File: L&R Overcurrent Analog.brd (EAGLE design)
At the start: 55 x 55 mm, 22 parts, among them IC1 CSLA2CFTH, IC2 TLC393CPN, IC3 7805TV, Q1 SUP75P0307, Q2 SUP75P0307, X1 J1

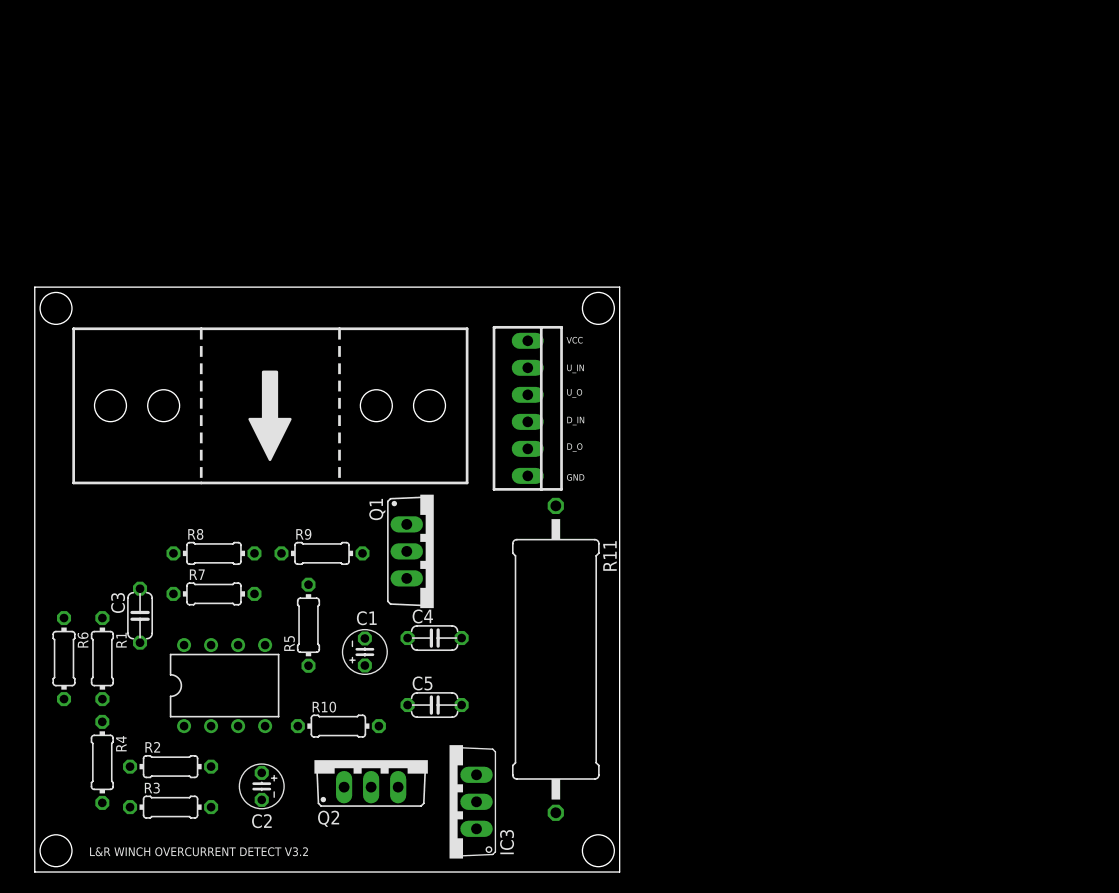
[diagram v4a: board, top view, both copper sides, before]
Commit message: Split transducer from main board, added schematic frame.
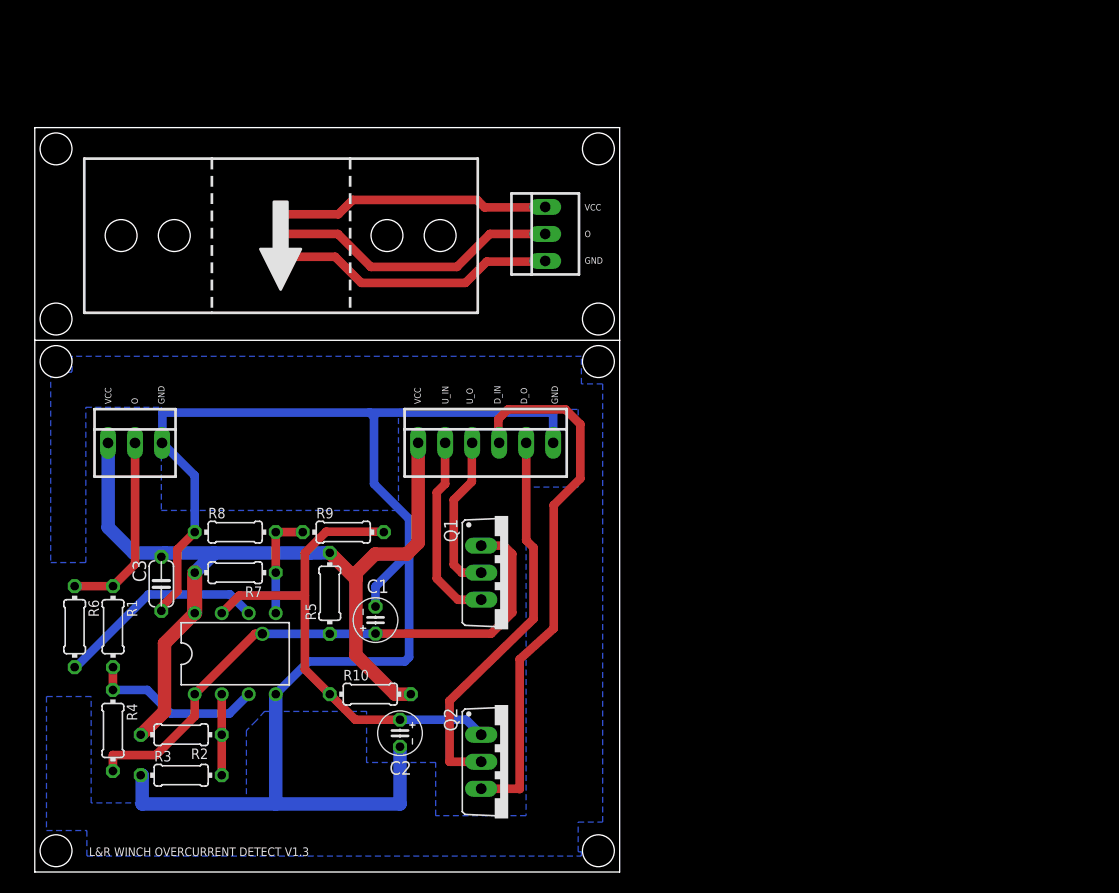
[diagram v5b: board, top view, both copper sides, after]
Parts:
- removed C4: 0.33u, Overcurrent Detect:C050-024X044
- removed C5: 0.1u, Overcurrent Detect:C050-024X044
- removed IC3: 7805TV, Overcurrent Detect:TO220V
- removed R11: 2, Overcurrent Detect:0617/22
- added X2: J2, Overcurrent Detect:22-23-2031
- added X3: J3, Overcurrent Detect:22-23-2031
- C1: value 20u -> 22u
- C2: value 20u -> 22u\
- moved IC1 16.0 mm to (23.1, 59.9)
- moved C2 13.9 mm to (34.3, 13.1)
- moved Q2 12.9 mm to (44.5, 10.4), turned to 270 degrees
- moved Q1 7.28 mm to (44.5, 28.1)
- moved X1 5.12 mm to (42.4, 40.4), turned to 0 degrees
- moved R10 4.24 mm to (31.6, 16.7)
- moved C3 3.61 mm to (11.9, 27.1)
- moved R5 3.61 mm to (27.7, 26.2)
- moved C1 3.16 mm to (32.0, 23.7)
- moved IC2 3.16 mm to (18.9, 20.5)
- moved R1 3.16 mm to (7.36, 23.1)
- moved R2 3.16 mm to (13.8, 12.9)
- moved R3 3.16 mm to (13.8, 9.10)
- moved R4 3.16 mm to (7.35, 13.3)
- moved R6 3.16 mm to (3.75, 23.1)
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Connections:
- removed net +5V: C3.1, C5.1, IC1.V+, IC2.8, IC3.3, R10.2, R2.2, R5.2, R7.2
- removed net N$3: IC1.O, R1.1, R6.1
- new net N$13: IC1.V-, X3.3
- new net N$14: IC1.O, X3.2
- new net N$15: R1.1, R6.1, X2.2
- net +12V: now also C3.1, IC2.8, R10.2, R2.2, R5.2, R7.2, X2.1; no longer R11.1
- net GND: now also X2.3; no longer C4.2, C5.2, IC1.V-, IC3.2
- net N$12: now also IC1.V+, X3.1; no longer C4.1, IC3.1, R11.2
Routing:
- net GND: track 0.00 -> 148.5 mm
- net +12V: track 0.00 -> 84.6 mm
- net N$6: track 0.00 -> 54.6 mm, vias 0 -> 1
- net N$10: track 0.00 -> 51.3 mm
- net N$7: track 0.00 -> 46.9 mm
- net N$11: track 0.00 -> 36.6 mm
- net N$14: track 0.00 -> 27.5 mm
- net N$12: track 0.00 -> 26.7 mm
- net N$13: track 0.00 -> 25.7 mm
- net N$4: track 0.00 -> 19.9 mm
- net N$8: track 0.00 -> 18.1 mm
- net N$15: track 0.00 -> 17.9 mm
- net N$1: track 0.00 -> 16.6 mm
- net N$9: track 0.00 -> 15.1 mm
- net N$5: track 0.00 -> 10.2 mm
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- added copper zone on layer 16, net GND
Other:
- board size 55 x 55 mm -> 55 x 70 mm
- board text added: "L&R WINCH OVERCURRENT DETECT V1.3"
- board text added: "O"
- board text removed: "L&R WINCH OVERCURRENT DETECT V3.2"

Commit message: Updated / added document frames and added cutout to PCB
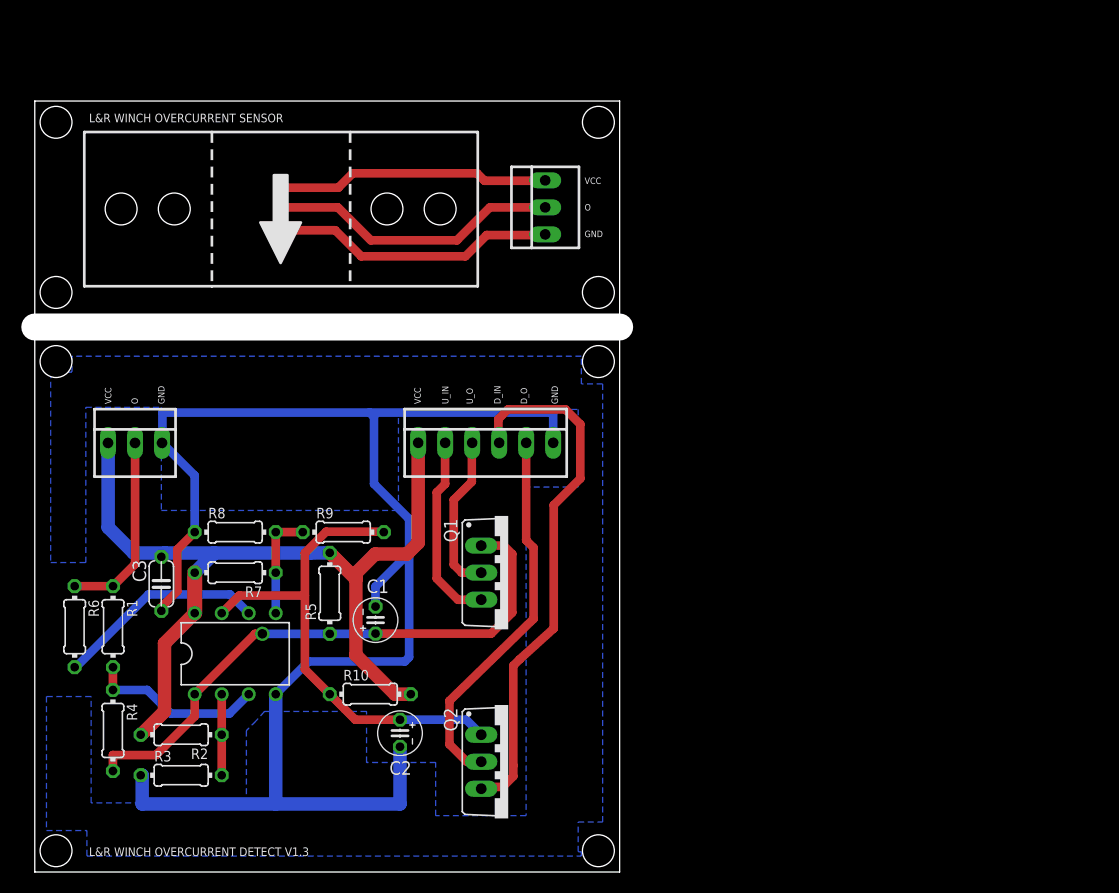
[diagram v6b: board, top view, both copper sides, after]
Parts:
- added FRAME1: (no value), L&R Overcurrent Analog:FRAME_A_L
- added U$1: DOCFIELD, L&R Overcurrent Analog:DOCFIELD
- moved IC1 2.50 mm to (23.1, 62.4)
- moved X3 2.50 mm to (48.0, 62.5)
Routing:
- net N$10: track 51.3 -> 50.2 mm
- net N$11: track 36.6 -> 35.6 mm
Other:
- board size 55 x 70 mm -> 55 x 72.5 mm
- board text added: "1/1"
- board text added: "CURRENT LIMIT BOARD FOR SIDE LAUNCH AND RECOVERY WINCH."
- board text added: "L&R WINCH OVERCURRENT SENSOR"
- board text added: "N/A"
- board text added: "v1.3"

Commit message: Minor updates to silkscreen, added cutout to PCB
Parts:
- IC1: value CSLA2CFTH -> TLC393CPN; device Overcurrent Detect:CSLA2CF -> Overcurrent Detect:DIL08
- IC2: value TLC393CPN -> CSLA2CFTH; device Overcurrent Detect:DIL08 -> Overcurrent Detect:CSLA2CF
- moved IC1 42.0 mm to (18.9, 20.5)
- moved IC2 42.0 mm to (23.1, 62.4)
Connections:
- net +12V: now also IC1.8; no longer IC2.8
- net GND: now also IC1.4; no longer IC2.4
- net N$1: now also IC1.3; no longer IC2.3
- net N$12: now also IC2.V+; no longer IC1.V+
- net N$13: now also IC2.V-; no longer IC1.V-
- net N$14: now also IC2.O; no longer IC1.O
- net N$2: now also IC1.2; no longer IC2.2
- net N$4: now also IC1.6; no longer IC2.6
- net N$5: now also IC1.5; no longer IC2.5
- net N$6: now also IC1.1; no longer IC2.1
- net N$7: now also IC1.7; no longer IC2.7
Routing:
- net GND: track 148.5 -> 146.8 mm
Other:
- outline, holes or cut-outs redrawn
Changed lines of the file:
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@@
 <wire x1="0" y1="0" x2="55" y2="0" width="0" layer="20"/>
 <wire x1="55" y1="0" x2="55" y2="51.25" width="0" layer="20"/>
-<wire x1="55" y1="51.25" x2="0" y2="51.25" width="2.54" layer="20"/>
 <wire x1="0" y1="51.25" x2="0" y2="0" width="0" layer="20"/>
 <text x="5.1" y="1.5" size="0.8128" layer="21">L&amp;R WINCH OVERCURRENT DETECT V1.3</text>
@@
 <text x="152.4" y="-77.724" size="2.54" layer="48">1/1</text>
 <text x="5.1" y="70.5" size="0.8128" layer="21">L&amp;R WINCH OVERCURRENT SENSOR</text>
+<wire x1="53.75" y1="51.25" x2="1.25" y2="51.25" width="2.54" layer="20"/>
 </plain>
 <attributes>
@@
 </autorouter>
 <elements>
-<element name="IC1" library="Overcurrent Detect" package="CSLA2CF" value="CSLA2CFTH" x="23.12" y="62.35" smashed="yes"/>
-<element name="IC2" library="Overcurrent Detect" package="DIL08" value="TLC393CPN" x="18.85" y="20.53" smashed="yes"/>
-<element name="R1" library="Overcurrent Detect" package="0204/7" value="3k" x="7.36" y="23.07" rot="R270"/>
-<element name="R2" library="Overcurrent Detect" package="0204/7" value="10k" x="13.77" y="12.91" rot="R180"/>
-<element name="R3" library="Overcurrent Detect" package="0204/7" value="24k" x="13.77" y="9.1"/>
-<element name="R4" library="Overcurrent Detect" package="0204/7" value="1M" x="7.35" y="13.31" rot="R270"/>
-<element name="R5" library="Overcurrent Detect" package="0204/7" value="10k" x="27.74" y="26.206259375" rot="R90"/>
-<element name="R6" library="Overcurrent Detect" package="0204/7" value="3k" x="3.75" y="23.07" rot="R270"/>
-<element name="R7" library="Overcurrent Detect" package="0204/7" value="15k" x="18.85" y="28.15" rot="R180"/>
-<element name="R8" library="Overcurrent Detect" package="0204/7" value="6.2k" x="18.85" y="31.96"/>
-<element name="R9" library="Overcurrent Detect" package="0204/7" value="1M" x="29.01" y="31.96"/>
-<element name="R10" library="Overcurrent Detect" package="0204/7" value="10k" x="31.55" y="16.72"/>
+<element name="IC2" library="Overcurrent Detect" package="CSLA2CF" value="CSLA2CFTH" x="23.12" y="62.35" smashed="yes"/>
+<element name="IC1" library="Overcurrent Detect" package="DIL08" value="TLC393CPN" x="18.85" y="20.53" smashed="yes">
+<attribute name="NAME" x="13.516" y="17.609" size="1.27" layer="25" ratio="10" rot="R90"/>
+</element>
+<element name="R1" library="Overcurrent Detect" package="0204/7" value="3k" x="7.36" y="23.07" smashed="yes" rot="R270">
+<attribute name="NAME" x="8.6554" y="25.61" size="0.9906" layer="25" ratio="10" rot="R270"/>
+</element>
+<element name="R2" library="Overcurrent Detect" package="0204/7" value="10k" x="13.77" y="12.91" smashed="yes" rot="R180">
+<attribute name="NAME" x="16.31" y="11.6146" size="0.9906" layer="25" ratio="10" rot="R180"/>
+</element>
+<element name="R3" library="Overcurrent Detect" package="0204/7" value="24k" x="13.77" y="9.1" smashed="yes">
+<attribute name="NAME" x="11.23" y="10.3954" size="0.9906" layer="25" ratio="10"/>
+</element>
+<element name="R4" library="Overcurrent Detect" package="0204/7" value="1M" x="7.35" y="13.31" smashed="yes" rot="R270">
+<attribute name="NAME" x="8.6454" y="15.85" size="0.9906" layer="25" ratio="10" rot="R270"/>
+</element>
+<element name="R5" library="Overcurrent Detect" package="0204/7" value="10k" x="27.74" y="26.206259375" smashed="yes" rot="R90">
+<attribute name="NAME" x="26.4446" y="23.666259375" size="0.9906" layer="25" ratio="10" rot="R90"/>
+</element>
+<element name="R6" library="Overcurrent Detect" package="0204/7" value="3k" x="3.75" y="23.07" smashed="yes" rot="R270">
+<attribute name="NAME" x="5.0454" y="25.61" size="0.9906" layer="25" ratio="10" rot="R270"/>
+</element>
+<element name="R7" library="Overcurrent Detect" package="0204/7" value="15k" x="18.85" y="28.15" smashed="yes" rot="R180">
+<attribute name="NAME" x="21.39" y="26.8546" size="0.9906" layer="25" ratio="10" rot="R180"/>
+</element>
+<element name="R8" library="Overcurrent Detect" package="0204/7" value="6.2k" x="18.85" y="31.96" smashed="yes">
+<attribute name="NAME" x="16.31" y="33.2554" size="0.9906" layer="25" ratio="10"/>
+</element>
+<element name="R9" library="Overcurrent Detect" package="0204/7" value="1M" x="29.01" y="31.96" smashed="yes">
+<attribute name="NAME" x="26.47" y="33.2554" size="0.9906" layer="25" ratio="10"/>
+</element>
+<element name="R10" library="Overcurrent Detect" package="0204/7" value="10k" x="31.55" y="16.72" smashed="yes">
+<attribute name="NAME" x="29.01" y="18.0154" size="0.9906" layer="25" ratio="10"/>
+</element>
 <element name="Q1" library="Overcurrent Detect" package="TO220BV" value="SUP75P0307" x="44.52" y="28.15" smashed="yes" rot="R270">
 <attribute name="NAME" x="38.4748" y="33.23" size="1.27" layer="25" ratio="10" rot="R270"/>
@@
 <contactref element="R5" pad="2"/>
 <contactref element="X1" pad="1"/>
-<contactref element="IC2" pad="8"/>
+<contactref element="IC1" pad="8"/>
 <wire x1="27.74" y1="30.016259375" x2="25.89" y2="30" width="1.27" layer="16"/>
 <wire x1="16.89" y1="30" x2="15.04" y2="28.15" width="1.27" layer="16"/>
@@
 <contactref element="R8" pad="1"/>
 <contactref element="X1" pad="6"/>
-<contactref element="IC2" pad="4"/>
+<contactref element="IC1" pad="4"/>
 <wire x1="22.66" y1="16.72" x2="22.66" y2="6.4" width="1.27" layer="16"/>
 <wire x1="22.66" y1="6.4" x2="10.1" y2="6.4" width="1.27" layer="16"/>
@@
 <contactref element="X2" pad="3"/>
 <contactref element="C3" pad="2"/>
-<wire x1="11.9682625" y1="40.350846875" x2="15.04" y2="37.279109375" width="0.8128" layer="16"/>
 <wire x1="15.04" y1="37.279109375" x2="15.04" y2="31.96" width="0.8128" layer="16"/>
 <wire x1="48.75" y1="40.36" x2="48.75" y2="43.2" width="0.8128" layer="16"/>
 <wire x1="48.75" y1="43.2" x2="31.5" y2="43.2" width="0.8128" layer="16"/>
-<wire x1="31.5" y1="43.2" x2="12" y2="43.2" width="0.8128" layer="16"/>
-<wire x1="12" y1="43.2" x2="12" y2="40.350846875" width="0.8128" layer="16"/>
 <wire x1="12" y1="40.350846875" x2="11.9682625" y2="40.350846875" width="0.8128" layer="16"/>
 <wire x1="32.042" y1="24.96" x2="32.042" y2="26.842" width="0.8128" layer="16"/>
@@
 <vertex x="4.8" y="29.1"/>
 <vertex x="4.8" y="43.7"/>
-<vertex x="11.9" y="43.7"/>
-<vertex x="11.9" y="34"/>
+<vertex x="13.9" y="43.7"/>
+<vertex x="13.9" y="34"/>
 <vertex x="34.2" y="34"/>
 <vertex x="34.2" y="43.5"/>
@@
 <vertex x="51.4" y="45.9"/>
 </polygon>
+<wire x1="31.5" y1="43.2" x2="20.960890625" y2="43.2" width="0.8128" layer="16"/>
+<wire x1="20.960890625" y1="43.2" x2="15.04" y2="37.279109375" width="0.8128" layer="16"/>
+<wire x1="15.04" y1="37.279109375" x2="15.04" y2="40.350846875" width="0.8128" layer="16"/>
+<wire x1="15.04" y1="40.350846875" x2="11.9682625" y2="40.350846875" width="0.8128" layer="16"/>
 </signal>
 <signal name="N$1">
 <contactref element="R1" pad="2"/>
-<contactref element="IC2" pad="3"/>
+<contactref element="IC1" pad="3"/>
 <contactref element="R4" pad="1"/>
 <wire x1="7.36" y1="19.26" x2="7.35" y2="19.25" width="0.8128" layer="1"/>
@@
 <contactref element="R3" pad="2"/>
 <contactref element="R2" pad="1"/>
-<contactref element="IC2" pad="2"/>
+<contactref element="IC1" pad="2"/>
 <wire x1="17.58" y1="9.1" x2="17.58" y2="12.91" width="0.8128" layer="1"/>
 <wire x1="17.58" y1="16.72" x2="17.58" y2="12.91" width="0.8128" layer="1"/>
@@
 <signal name="N$4">
 <contactref element="R6" pad="2"/>
-<contactref element="IC2" pad="6"/>
+<contactref element="IC1" pad="6"/>
 <wire x1="20.12" y1="24.34" x2="18.36" y2="26.1" width="0.8128" layer="16"/>
 <wire x1="18.36" y1="26.1" x2="10.7" y2="26.1" width="0.8128" layer="16"/>
@@
 <contactref element="R7" pad="1"/>
 <contactref element="R8" pad="2"/>
-<contactref element="IC2" pad="5"/>
+<contactref element="IC1" pad="5"/>
 <contactref element="R9" pad="1"/>
 <wire x1="22.66" y1="28.15" x2="22.66" y2="31.96" width="0.8128" layer="1"/>
@@
 <signal name="N$6">
 <contactref element="R4" pad="2"/>
-<contactref element="IC2" pad="1"/>
+<contactref element="IC1" pad="1"/>
 <contactref element="Q1" pad="G"/>
 <contactref element="R5" pad="1"/>
@@
 <signal name="N$7">
 <contactref element="R9" pad="2"/>
-<contactref element="IC2" pad="7"/>
+<contactref element="IC1" pad="7"/>
 <contactref element="Q2" pad="G"/>
 <contactref element="R10" pad="1"/>
@@
 </signal>
 <signal name="N$12">
-<contactref element="IC1" pad="V+"/>
+<contactref element="IC2" pad="V+"/>
 <contactref element="X3" pad="1"/>
 <wire x1="23.12" y1="60.35" x2="28.25" y2="60.35" width="0.8128" layer="1"/>
@@
 </signal>
 <signal name="N$13">
-<contactref element="IC1" pad="V-"/>
+<contactref element="IC2" pad="V-"/>
 <contactref element="X3" pad="3"/>
 <wire x1="23.12" y1="64.35" x2="28.55" y2="64.35" width="0.8128" layer="1"/>
@@
 </signal>
 <signal name="N$14">
-<contactref element="IC1" pad="O"/>
+<contactref element="IC2" pad="O"/>
 <contactref element="X3" pad="2"/>
 <wire x1="23.27" y1="62.5" x2="23.12" y2="62.35" width="0.8128" layer="1"/>
